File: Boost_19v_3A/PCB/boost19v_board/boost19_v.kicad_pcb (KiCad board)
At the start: 2 copper layers, 19 parts, among them J1 8P4C, U1 TPS55340QRTERQ1

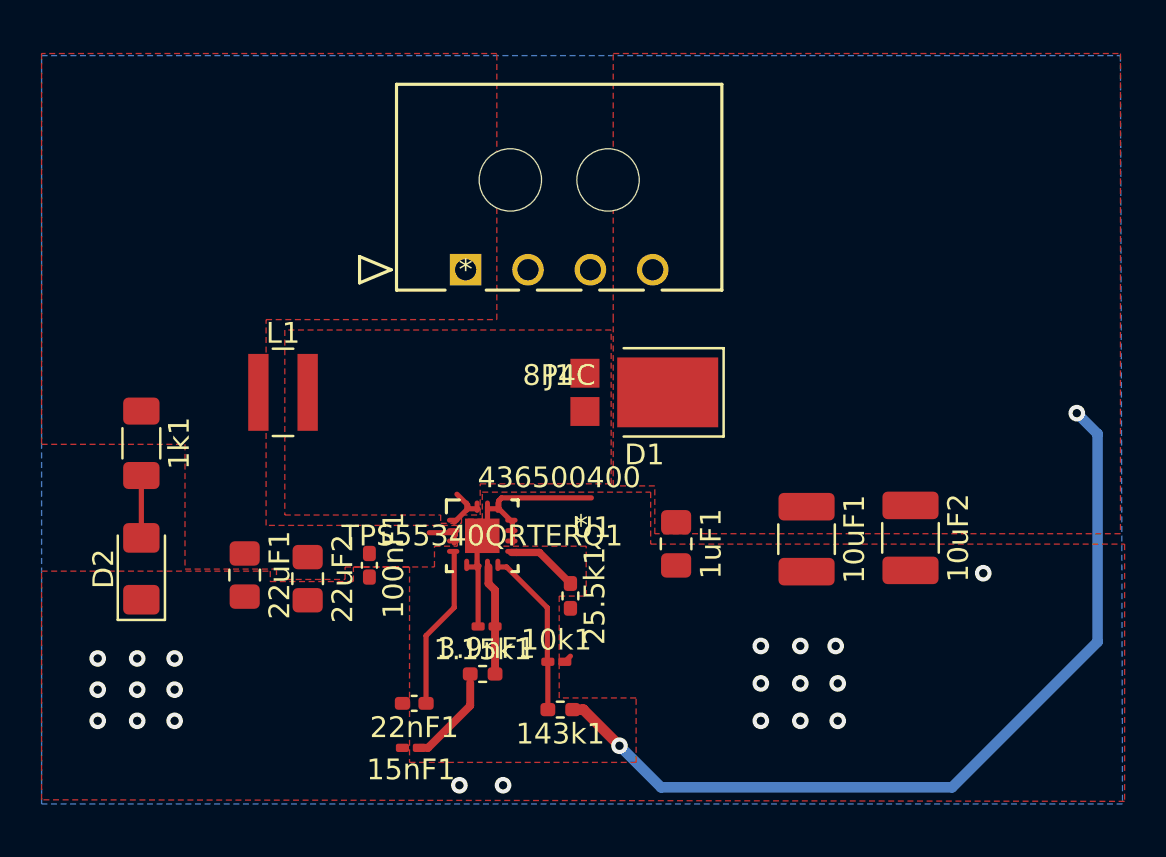
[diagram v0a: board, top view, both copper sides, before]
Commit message: minor fixes, size reduced
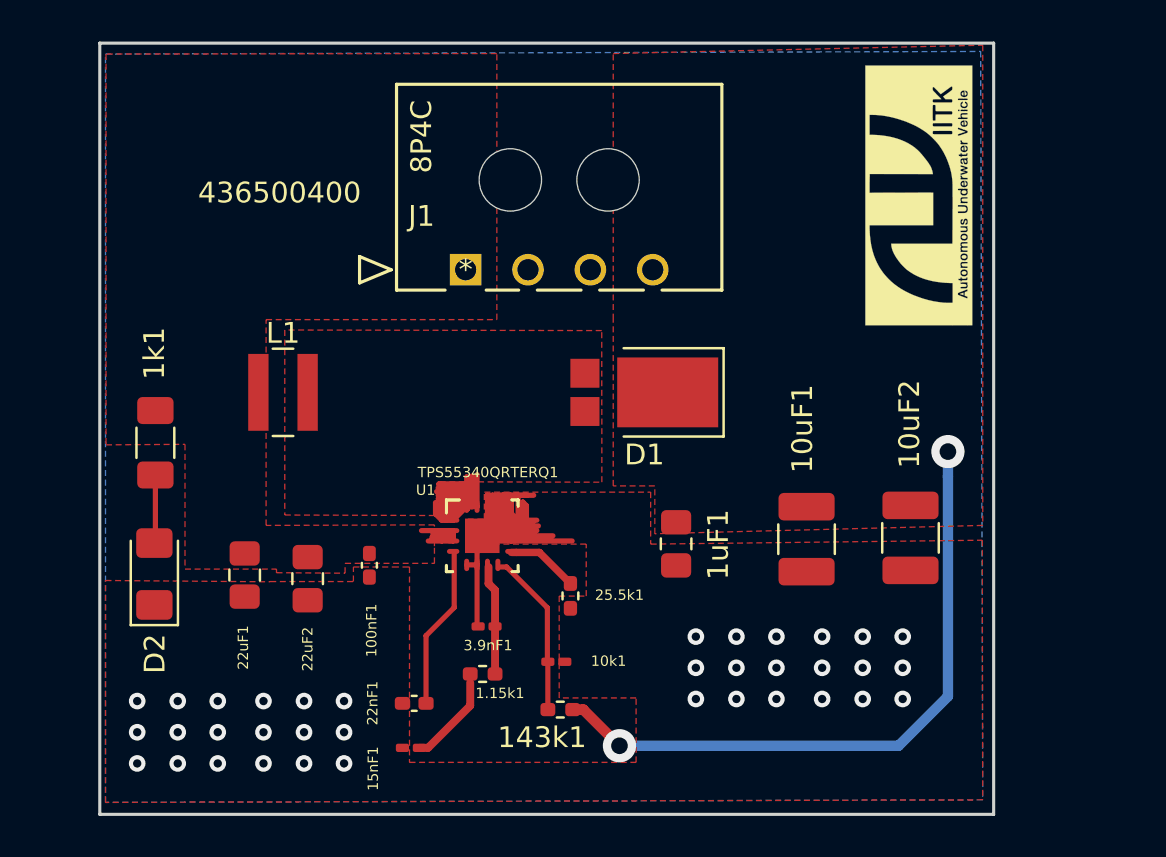
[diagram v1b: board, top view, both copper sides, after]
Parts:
- added G***: LOGO, AUV Logo:auv_logo_small, F.Cu at (153.4, 80.5)
- moved 1k1 0.68 mm to (116.7, 92.4)
- moved D2 0.67 mm to (116.6, 98.7)
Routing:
- net Net-(100nF1-Pad2): track 14.2 -> 41.6 mm, vias 21 -> 36
- net Net-(D1-Pad2): track 2.33 -> 21.8 mm
- net Net-(10uF1-Pad1): track 41.1 -> 31.5 mm
- net Net-(100nF1-Pad1): track 1.70 -> 5.23 mm
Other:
- board outline added: 43 x 37.1 mm
- net class Default: clearance 0.2 -> 0.1
- rule trace_clearance: 0.2 -> 0.1
